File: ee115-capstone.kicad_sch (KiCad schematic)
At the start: 13 parts, among them J2 9V_BATTERY, Q1 PMOS, Q2 NMOS, SW3 SW_Push

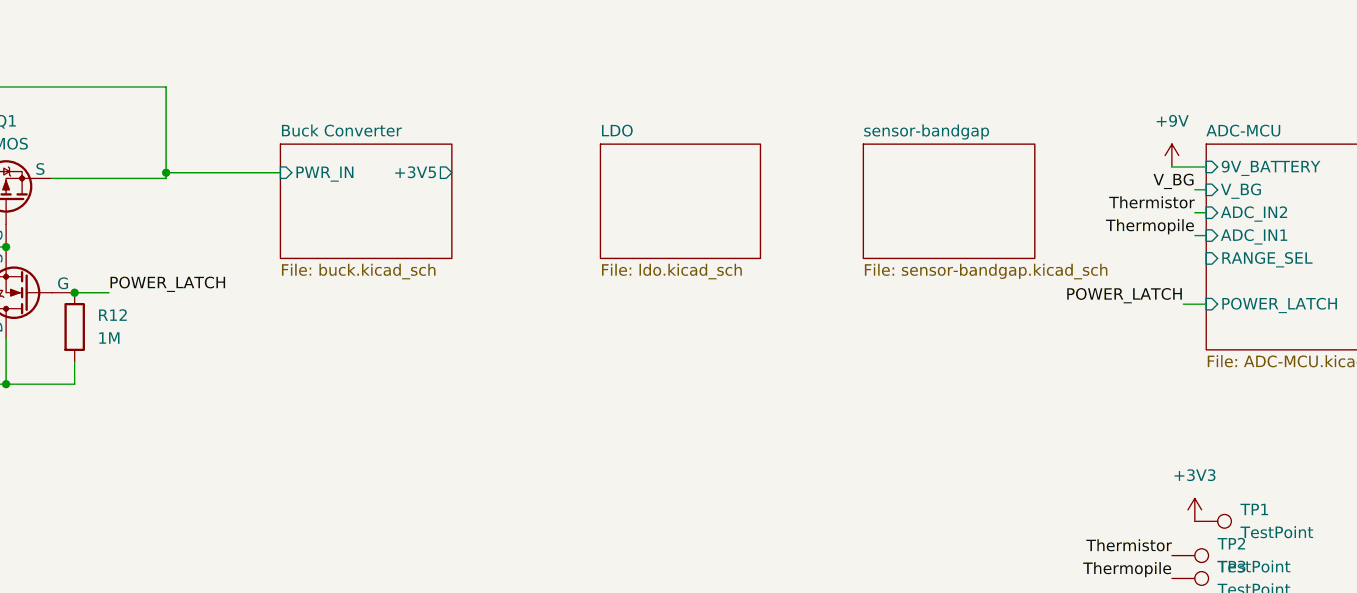
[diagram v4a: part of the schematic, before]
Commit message: ldo and buck updated, footprints added
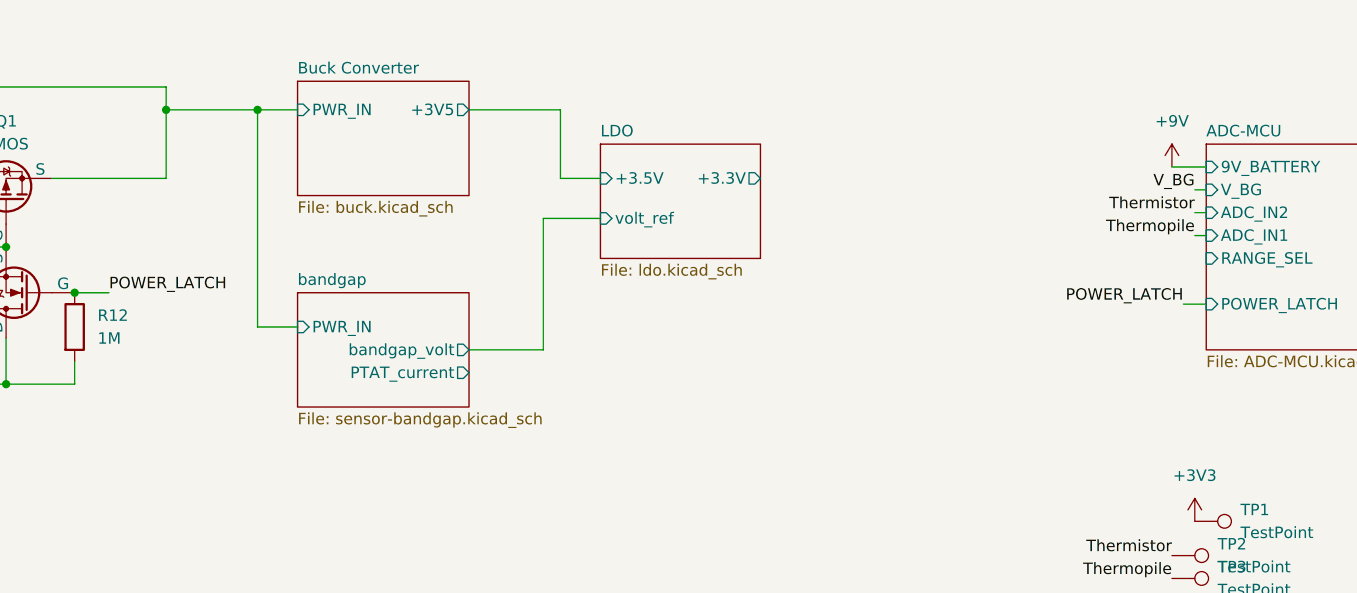
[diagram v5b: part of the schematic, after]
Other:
- sheet sensor-bandgap renamed bandgap
- sheet LDO ports: added +3.3V, +3.5V, volt_ref; removed none
- sheet bandgap ports: added PTAT_current, PWR_IN, bandgap_volt; removed none
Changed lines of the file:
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@@
-	)
-	(junction
-		(at 77.47 62.865)
-		(diameter 0)
-		(color 0 0 0 0)
 	)
 	(junction
@@
 	)
 	(junction
+		(at 77.47 55.88)
+		(diameter 0)
+		(color 0 0 0 0)
+	)
+	(junction
 		(at 43.18 63.5)
+		(diameter 0)
+		(color 0 0 0 0)
+	)
+	(junction
+		(at 87.63 55.88)
 		(diameter 0)
 		(color 0 0 0 0)
@@
 	(wire
 		(pts
+			(xy 121.285 55.88) (xy 121.285 63.5)
+		)
+		(stroke
+			(width 0)
+			(type default)
+		)
+	)
+	(wire
+		(pts
+			(xy 111.125 82.55) (xy 119.38 82.55)
+		)
+		(stroke
+			(width 0)
+			(type default)
+		)
+	)
+	(wire
+		(pts
+			(xy 87.63 55.88) (xy 92.075 55.88)
+		)
+		(stroke
+			(width 0)
+			(type default)
+		)
+	)
+	(wire
+		(pts
 			(xy 191.77 67.31) (xy 193.04 67.31)
 		)
@@
 	(wire
 		(pts
-			(xy 77.47 62.865) (xy 77.47 63.5)
-		)
-		(stroke
-			(width 0)
-			(type default)
-		)
-	)
-	(wire
-		(pts
 			(xy 31.75 52.07) (xy 31.75 53.34)
 		)
@@
 	(wire
 		(pts
+			(xy 121.285 63.5) (xy 125.73 63.5)
+		)
+		(stroke
+			(width 0)
+			(type default)
+		)
+	)
+	(wire
+		(pts
 			(xy 71.12 76.2) (xy 67.31 76.2)
 		)
@@
 	(wire
 		(pts
+			(xy 119.38 67.945) (xy 125.73 67.945)
+		)
+		(stroke
+			(width 0)
+			(type default)
+		)
+	)
+	(wire
+		(pts
 			(xy 48.26 71.12) (xy 59.69 71.12)
 		)
@@
 	(wire
 		(pts
-			(xy 77.47 62.865) (xy 90.17 62.865)
+			(xy 77.47 55.88) (xy 87.63 55.88)
+		)
+		(stroke
+			(width 0)
+			(type default)
+		)
+	)
+	(wire
+		(pts
+			(xy 87.63 80.01) (xy 92.075 80.01)
 		)
 		(stroke
@@
 	(wire
 		(pts
+			(xy 111.125 55.88) (xy 121.285 55.88)
+		)
+		(stroke
+			(width 0)
+			(type default)
+		)
+	)
+	(wire
+		(pts
 			(xy 67.31 86.36) (xy 59.69 86.36)
 		)
@@
 	(wire
 		(pts
+			(xy 119.38 82.55) (xy 119.38 67.945)
+		)
+		(stroke
+			(width 0)
+			(type default)
+		)
+	)
+	(wire
+		(pts
 			(xy 48.26 63.5) (xy 54.61 63.5)
 		)
@@
 	(wire
 		(pts
-			(xy 77.47 53.34) (xy 77.47 62.865)
+			(xy 77.47 55.88) (xy 77.47 63.5)
+		)
+		(stroke
+			(width 0)
+			(type default)
+		)
+	)
+	(wire
+		(pts
+			(xy 77.47 53.34) (xy 77.47 55.88)
+		)
+		(stroke
+			(width 0)
+			(type default)
+		)
+	)
+	(wire
+		(pts
+			(xy 87.63 55.88) (xy 87.63 80.01)
 		)
 		(stroke
@@
 	)
 	(sheet
-		(at 90.17 59.69)
+		(at 92.075 52.705)
 		(size 19.05 12.7)
 		(exclude_from_sim no)
@@
 		)
 		(property "Sheetname" "Buck Converter"
-			(at 90.17 58.9784 0)
+			(at 92.075 51.9934 0)
 			(effects
 				(font
@@
 		)
 		(property "Sheetfile" "buck.kicad_sch"
-			(at 90.17 72.9746 0)
+			(at 92.075 65.9896 0)
 			(effects
 				(font
@@
 		)
 		(pin "PWR_IN" input
-			(at 90.17 62.865 180)
+			(at 92.075 55.88 180)
 			(effects
 				(font
@@
 		)
 		(pin "+3V5" output
-			(at 109.22 62.865 0)
+			(at 111.125 55.88 0)
 			(effects
 				(font
@@
 			)
 		)
+		(pin "+3.3V" output
+			(at 143.51 63.5 0)
+			(effects
+				(font
+					(size 1.27 1.27)
+				)
+				(justify right)
+			)
+		)
+		(pin "+3.5V" input
+			(at 125.73 63.5 180)
+			(effects
+				(font
+					(size 1.27 1.27)
+				)
+				(justify left)
+			)
+		)
+		(pin "volt_ref" input
+			(at 125.73 67.945 180)
+			(effects
+				(font
+					(size 1.27 1.27)
+				)
+				(justify left)
+			)
+		)
 		(instances
 			(project "ee115-capstone"
@@
 	)
 	(sheet
-		(at 154.94 59.69)
+		(at 92.075 76.2)
 		(size 19.05 12.7)
 		(exclude_from_sim no)
@@
 			(color 0 0 0 0.0000)
 		)
-		(property "Sheetname" "sensor-bandgap"
-			(at 154.94 58.9784 0)
+		(property "Sheetname" "bandgap"
+			(at 92.075 75.4884 0)
 			(effects
 				(font
@@
 		)
 		(property "Sheetfile" "sensor-bandgap.kicad_sch"
-			(at 154.94 72.9746 0)
+			(at 92.075 89.4846 0)
 			(effects
 				(font
@@
 			)
 		)
+		(pin "PWR_IN" input
+			(at 92.075 80.01 180)
+			(effects
+				(font
+					(size 1.27 1.27)
+				)
+				(justify left)
+			)
+		)
+		(pin "bandgap_volt" output
+			(at 111.125 82.55 0)
+			(effects
+				(font
+					(size 1.27 1.27)
+				)
+				(justify right)
+			)
+		)
+		(pin "PTAT_current" output
+			(at 111.125 85.09 0)
+			(effects
+				(font
+					(size 1.27 1.27)
+				)
+				(justify right)
+			)
+		)

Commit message: schematic cleanup
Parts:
- added J5: Conn_01x03_Pin, Connector_JST:JST_PH_S3B-PH-K_1x03_P2.00mm_Horizontal, symbol Connector:Conn_01x03_Pin
- added J6: Conn_02x02_Odd_Even, Connector_Molex:Molex_Mega-Fit_76829-0004_2x02_P5.70mm_Vertical, symbol Connector_Generic:Conn_02x02_Odd_Even
- Q1: footprint (none) -> Package_TO_SOT_THT:TO-220-3_Horizontal_TabDown
- Q2: footprint (none) -> Package_TO_SOT_THT:TO-92
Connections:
- net +3V3: now also J5.1 (Pin_1)
- net GND: now also J5.3 (Pin_3), J6.3 (Pin_3), J6.4 (Pin_4)
- net Thermistor: now also J6.1 (Pin_1)
- net Thermopile: now also J6.2 (Pin_2)
- net Buck Converter/PWR_IN renamed PWR_IN
- new net RANGE_SEL: J5.2 (Pin_2)
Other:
- sheet Buck Converter ports: added I_PTAT; removed none
- sheet LDO ports: added PWR_IN; removed none

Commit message: pcb layout
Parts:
- TP1, TP2, TP3, TP4: footprint Connector_Pin:Pin_D1.0mm_L10.0mm -> TestPoint:TestPoint_Plated_Hole_D2.0mm
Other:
- sheet Buck Converter ports: added bg_volt; removed none
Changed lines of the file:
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@@
 	(paper "A4")
+	(junction
+		(at 120.015 67.31)
+		(diameter 0)
+		(color 0 0 0 0)
+	)
 	(junction
 		(at 48.26 63.5)
@@
 	(wire
 		(pts
-			(xy 146.05 63.5) (xy 146.05 62.23)
+			(xy 149.225 63.5) (xy 149.225 62.23)
 		)
 		(stroke
@@
 	(wire
 		(pts
-			(xy 143.51 63.5) (xy 146.05 63.5)
-		)
-		(stroke
-			(width 0)
-			(type default)
-		)
-	)
-	(wire
-		(pts
 			(xy 114.3 78.74) (xy 114.3 62.23)
 		)
@@
 	(wire
 		(pts
+			(xy 146.685 63.5) (xy 149.225 63.5)
+		)
+		(stroke
+			(width 0)
+			(type default)
+		)
+	)
+	(wire
+		(pts
 			(xy 43.18 63.5) (xy 48.26 63.5)
 		)
@@
 	(wire
 		(pts
-			(xy 121.92 63.5) (xy 125.73 63.5)
+			(xy 121.92 63.5) (xy 125.857 63.5)
 		)
 		(stroke
@@
 	(wire
 		(pts
-			(xy 120.015 67.945) (xy 125.73 67.945)
+			(xy 120.015 67.31) (xy 125.857 67.31)
 		)
 		(stroke
@@
 	(wire
 		(pts
+			(xy 120.015 58.42) (xy 111.76 58.42)
+		)
+		(stroke
+			(width 0)
+			(type default)
+		)
+	)
+	(wire
+		(pts
 			(xy 77.47 55.88) (xy 87.63 55.88)
 		)
@@
 	(wire
 		(pts
-			(xy 125.73 71.12) (xy 124.46 71.12)
+			(xy 125.857 71.12) (xy 124.46 71.12)
 		)
 		(stroke
@@
 	(wire
 		(pts
+			(xy 120.015 67.31) (xy 120.015 58.42)
+		)
+		(stroke
+			(width 0)
+			(type default)
+		)
+	)
+	(wire
+		(pts
 			(xy 67.31 86.36) (xy 59.69 86.36)
 		)
@@
 	(wire
 		(pts
-			(xy 120.015 82.55) (xy 120.015 67.945)
+			(xy 120.015 67.31) (xy 120.015 82.55)
 		)
 		(stroke
@@
 			)
 		)
-		(property "Footprint" "Connector_Pin:Pin_D1.0mm_L10.0mm"
+		(property "Footprint" "TestPoint:TestPoint_Plated_Hole_D2.0mm"
 			(at 191.77 106.68 0)
 			(effects
@@
 			)
 		)
-		(property "Footprint" "Connector_Pin:Pin_D1.0mm_L10.0mm"
+		(property "Footprint" "TestPoint:TestPoint_Plated_Hole_D2.0mm"
 			(at 190.5 118.11 0)
 			(effects
@@
 	(symbol
 		(lib_id "power:+3V3")
-		(at 146.05 62.23 0)
+		(at 149.225 62.23 0)
 		(unit 1)
 		(exclude_from_sim no)
@@
 		(fields_autoplaced yes)
 		(property "Reference" "#PWR095"
-			(at 146.05 66.04 0)
+			(at 149.225 66.04 0)
 			(effects
 				(font
@@
 		)
 		(property "Value" "+3V3"
-			(at 146.05 57.15 0)
+			(at 149.225 57.15 0)
 			(effects
 				(font
@@
 		)
 		(property "Footprint" ""
-			(at 146.05 62.23 0)
+			(at 149.225 62.23 0)
 			(effects
 				(font
@@
 		)
 		(property "Datasheet" ""
-			(at 146.05 62.23 0)
+			(at 149.225 62.23 0)
 			(effects
 				(font
@@
 		)
 		(property "Description" "Power symbol creates a global label with name \"+3V3\""
-			(at 146.05 62.23 0)
+			(at 149.225 62.23 0)
 			(effects
 				(font
@@
 			)
 		)
-		(property "Footprint" "Connector_Pin:Pin_D1.0mm_L10.0mm"
+		(property "Footprint" "TestPoint:TestPoint_Plated_Hole_D2.0mm"
 			(at 189.23 113.03 0)
 			(effects
@@
 			)
 		)
-		(property "Footprint" "Connector_Pin:Pin_D1.0mm_L10.0mm"
+		(property "Footprint" "TestPoint:TestPoint_Plated_Hole_D2.0mm"
 			(at 189.23 110.49 0)
 			(effects
@@
 			)
 		)
+		(pin "bg_volt" input
+			(at 111.76 58.42 0)
+			(effects
+				(font
+					(size 1.27 1.27)
+				)
+				(justify right)
+			)
+		)
 		(instances
 			(project "ee115-capstone"
@@
 	)
 	(sheet
-		(at 125.73 59.69)
+		(at 125.857 59.69)
 		(size 20.828 16.002)
 		(exclude_from_sim no)
@@
 		)
 		(property "Sheetname" "LDO"
-			(at 125.73 58.9784 0)
+			(at 125.857 58.9784 0)
 			(effects
 				(font
@@
 		)
 		(property "Sheetfile" "ldo.kicad_sch"
-			(at 125.73 76.2766 0)
+			(at 125.857 76.2766 0)
 			(effects
 				(font
@@
 		)
 		(pin "+3.3V" output
-			(at 146.558 63.5 0)
+			(at 146.685 63.5 0)
 			(effects
 				(font
@@
 		)
 		(pin "+3.5V" input
-			(at 125.73 63.5 180)
+			(at 125.857 63.5 180)
 			(effects
 				(font
@@
 		)
 		(pin "volt_ref" input
-			(at 125.73 67.945 180)
+			(at 125.857 67.31 180)
 			(effects
 				(font
@@
 		)
 		(pin "PWR_IN" input
-			(at 125.73 71.12 180)
-			(effects
-				(font
+			(at 125.857 71.12 180)
+			(effects
+				(font

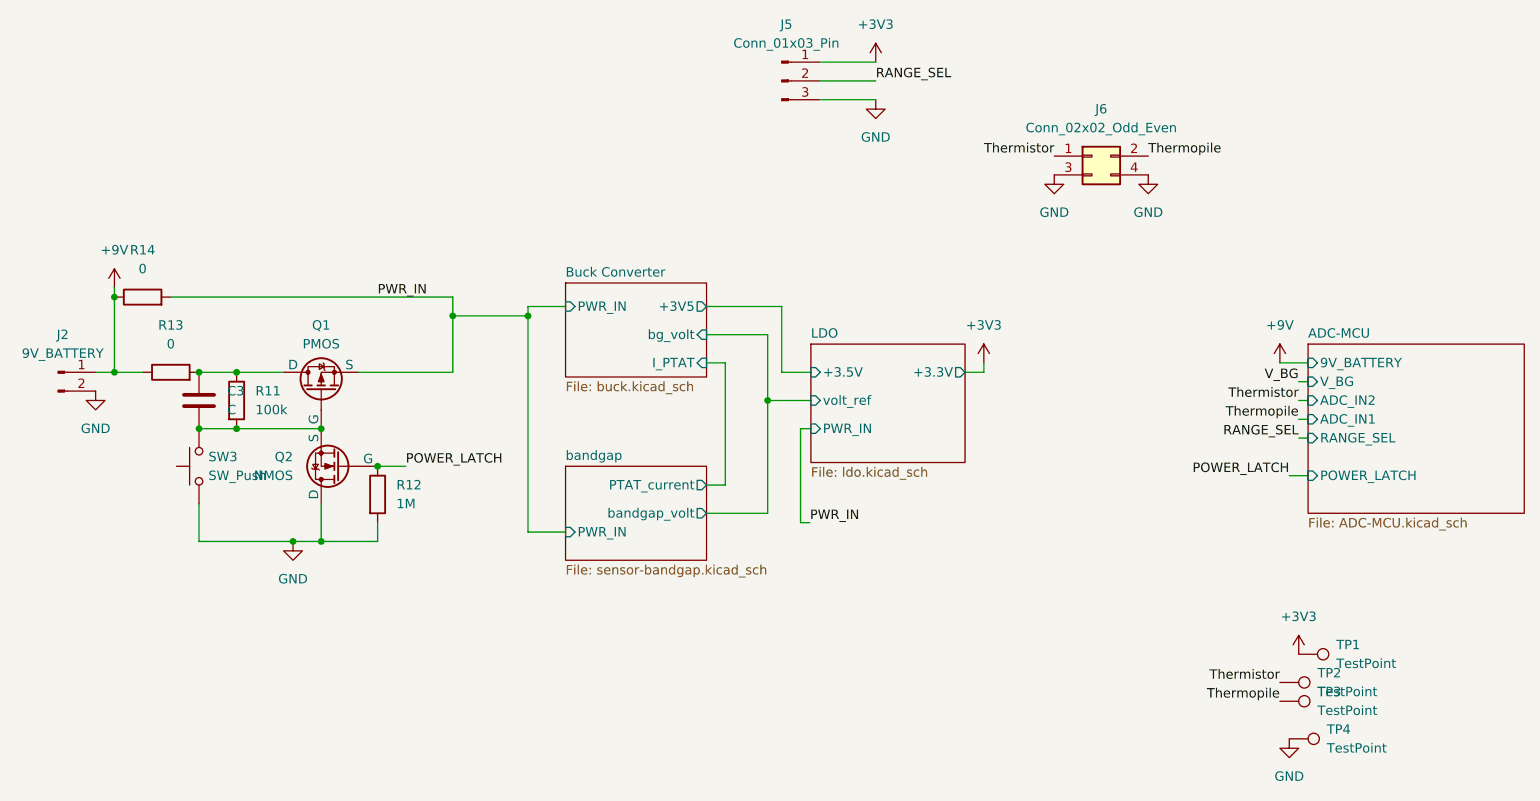
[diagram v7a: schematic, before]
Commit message: pcb layout component placement 90% done
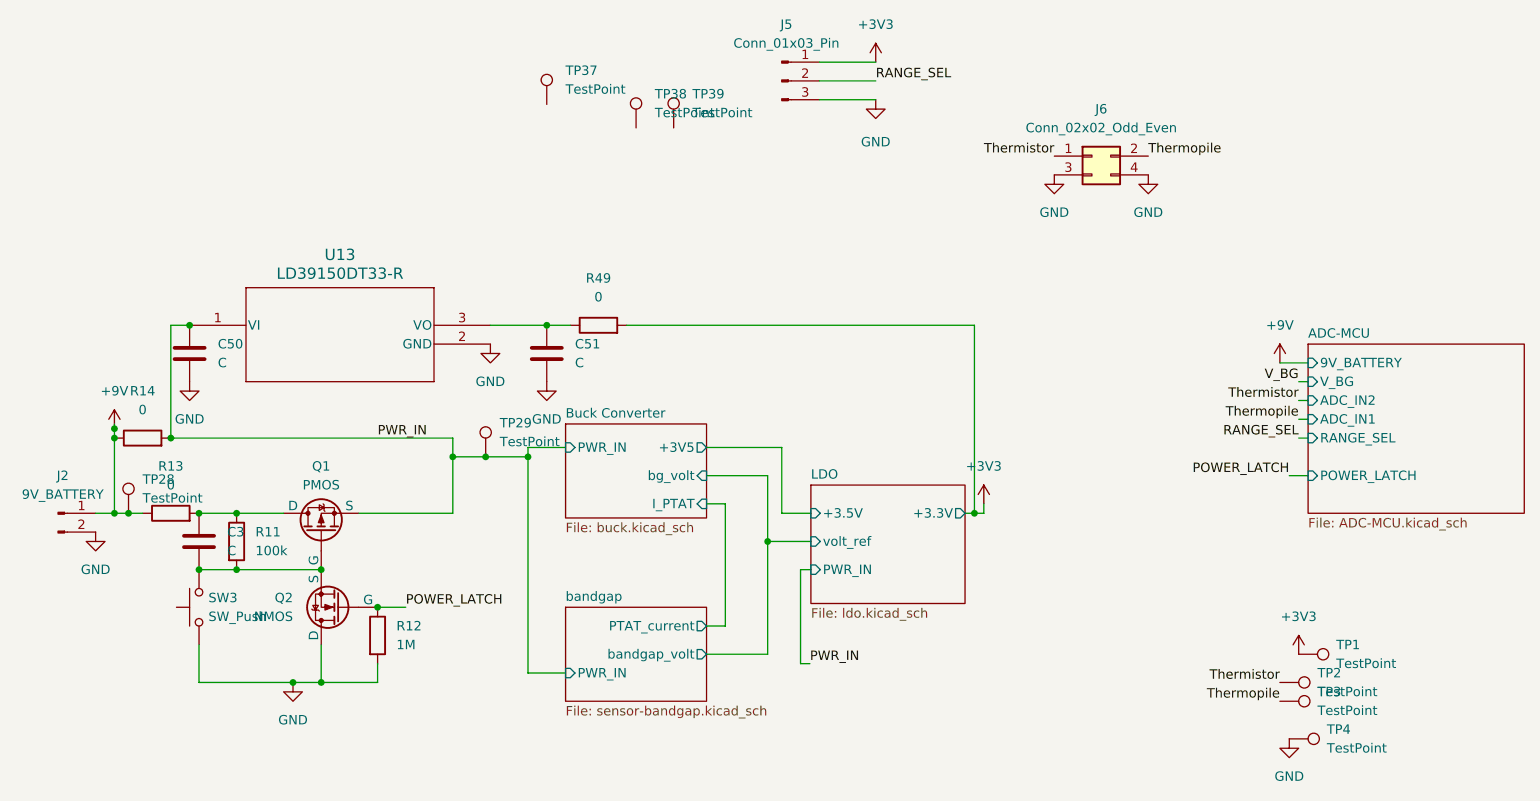
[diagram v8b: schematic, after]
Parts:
- added C50, C51: C, Capacitor_SMD:C_0805_2012Metric, symbol Device:C
- added R49: 0, Resistor_SMD:R_0805_2012Metric, symbol Device:R
- added TP28, TP29: TestPoint, TestPoint:TestPoint_Plated_Hole_D2.0mm, symbol Connector:TestPoint
- added TP37, TP38, TP39: TestPoint, MountingHole:MountingHole_3.2mm_M3, symbol Connector:TestPoint
- added U13: LD39150DT33-R, footprints_pretty:SOT_0DT33-R_STM, symbol LDO1111:LD39150DT33-R
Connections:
- net +3V3: now also R49.2
- net +9V: now also TP28.1
- net GND: now also C50.2, C51.2, U13.2 (GND)
- net PWR_IN: now also C50.1, TP29.1, U13.1 (VI)
- new net: C51.1, R49.1, U13.3 (VO)
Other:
- moved on the sheet: C3, J2, Q1, Q2, R11, R12, R13, R14, SW3
